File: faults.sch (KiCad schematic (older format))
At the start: 4 parts

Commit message: Adds todos.
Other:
- note added: "TODO(willjschmitt): Implement fault latching."
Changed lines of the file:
@@
 Wire Wire Line
 	5950 2000 6050 2000
+Text Notes 6700 1350 0    60   ~ 0
+TODO(willjschmitt): Implement fault latching.
 $EndSCHEMATC

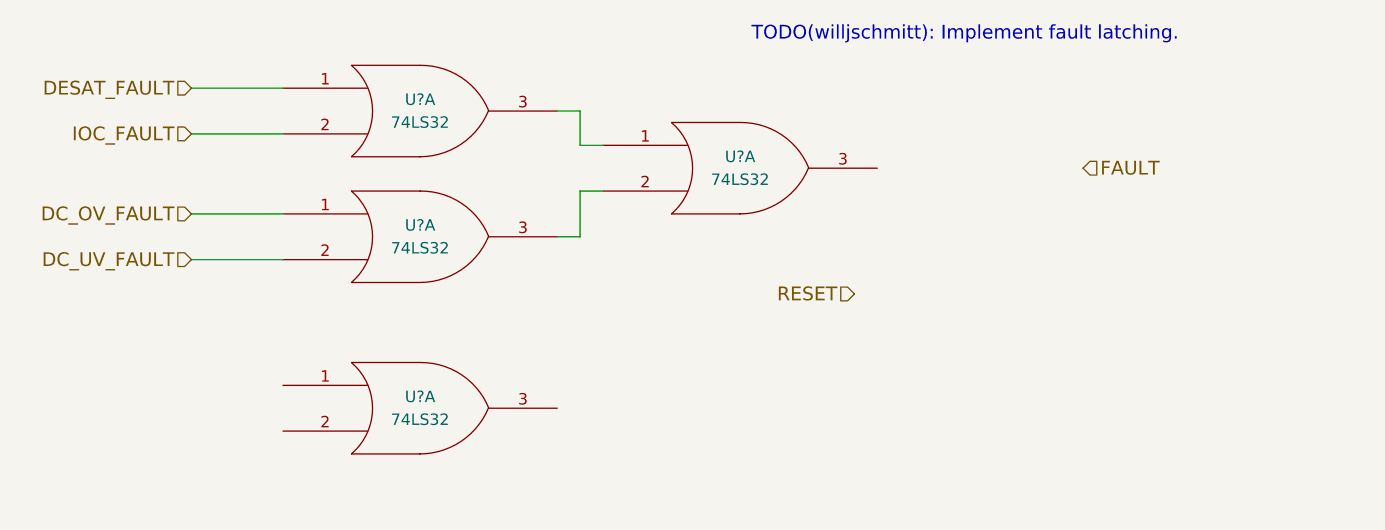
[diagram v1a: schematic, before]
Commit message: Adding latch to fault module.
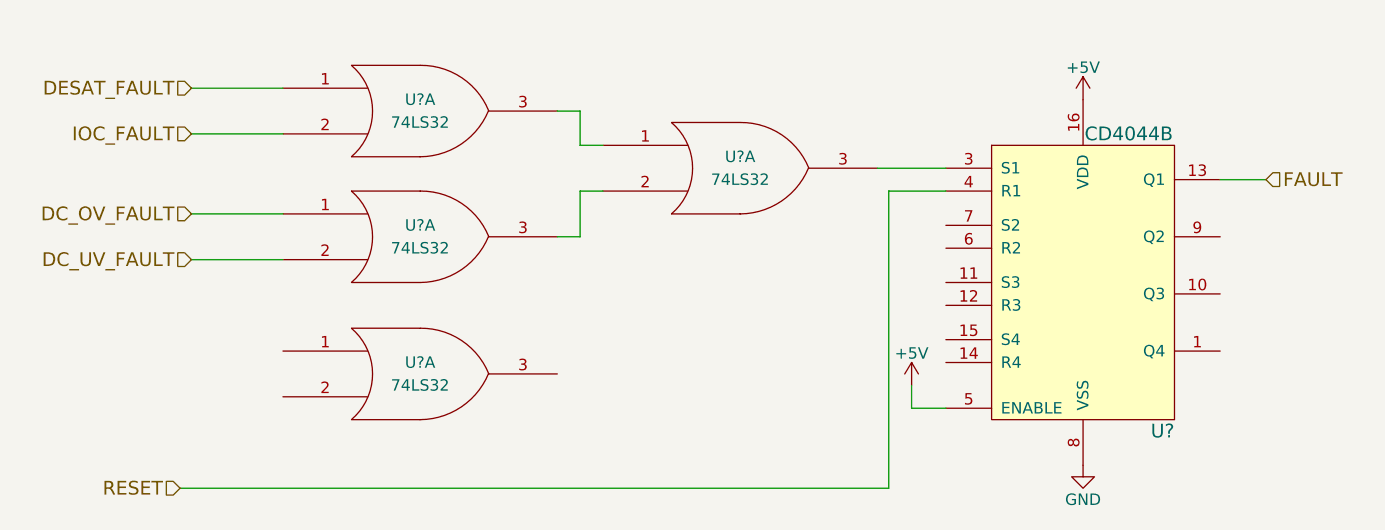
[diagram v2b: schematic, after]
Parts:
- added U?: CD4044B, symbol CD4044B
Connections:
- net FAULT: now also U?.13 (Q1)
- net GND: now also U?.8 (VSS)
- net RESET: now also U?.4 (R1)
- net at U?.3: now also U?.3 (S1)
- new net +5V: U?.16 (VDD), U?.5 (ENABLE)
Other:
- note removed: "TODO(willjschmitt): Implement fault latching."
- moved on the sheet: U?A
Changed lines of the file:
@@
 Text HLabel 4250 1550 0    60   Input ~ 0
 DESAT_FAULT
-Text HLabel 7150 2450 0    60   Input ~ 0
+Text HLabel 4200 3300 0    60   Input ~ 0
 RESET
-Text HLabel 8150 1900 2    60   Input ~ 0
+Text HLabel 8950 1950 2    60   Input ~ 0
 FAULT
 Text HLabel 4250 2100 0    60   Input ~ 0
@@
 L 74LS32 U?
 U 1 1 5AFAF32E
-P 5250 2950
-F 0 "U?" H 5250 3000 50  0000 C CNN
-F 1 "74LS32" H 5250 2900 50  0000 C CNN
-F 2 "" H 5250 2950 50  0001 C CNN
-F 3 "" H 5250 2950 50  0001 C CNN
-	1    5250 2950
+P 5250 2800
+F 0 "U?" H 5250 2850 50  0000 C CNN
+F 1 "74LS32" H 5250 2750 50  0000 C CNN
+F 2 "" H 5250 2800 50  0001 C CNN
+F 3 "" H 5250 2800 50  0001 C CNN
+	1    5250 2800
 	1    0    0    -1
 $EndComp
@@
 Wire Wire Line
 	5950 2000 6050 2000
-Text Notes 6700 1350 0    60   ~ 0
-TODO(willjschmitt): Implement fault latching.
+$Comp
+L CD4044B U?
+U 1 1 5AFE1E4B
+P 8150 2200
+F 0 "U?" H 8550 1350 60  0000 R CNN
+F 1 "CD4044B" H 8350 2650 60  0000 C CNN
+F 2 "" H 8150 2200 60  0001 C CNN
+F 3 "" H 8150 2200 60  0001 C CNN
+	1    8150 2200
+	1    0    0    -1
+$EndComp
+Wire Wire Line
+	4200 3300 7300 3300
+Wire Wire Line
+	7300 3300 7300 2000
+Wire Wire Line
+	7300 2000 7550 2000
+Wire Wire Line
+	7250 1900 7550 1900
+$Comp
+L +5V #PWR?
+U 1 1 5AFE2198
+P 8150 1600
+F 0 "#PWR?" H 8150 1450 50  0001 C CNN
+F 1 "+5V" H 8150 1740 50  0000 C CNN
+F 2 "" H 8150 1600 50  0001 C CNN
+F 3 "" H 8150 1600 50  0001 C CNN
+	1    8150 1600
+	1    0    0    -1
+$EndComp
+$Comp
+L GND #PWR?
+U 1 1 5AFE21F2
+P 8150 3200
+F 0 "#PWR?" H 8150 2950 50  0001 C CNN
+F 1 "GND" H 8150 3050 50  0000 C CNN
+F 2 "" H 8150 3200 50  0001 C CNN
+F 3 "" H 8150 3200 50  0001 C CNN
+	1    8150 3200
+	1    0    0    -1
+$EndComp
+Wire Wire Line
+	8950 1950 8750 1950
+$Comp
+L +5V #PWR?
+U 1 1 5AFE2A17
+P 7400 2850
+F 0 "#PWR?" H 7400 2700 50  0001 C CNN
+F 1 "+5V" H 7400 2990 50  0000 C CNN
+F 2 "" H 7400 2850 50  0001 C CNN
+F 3 "" H 7400 2850 50  0001 C CNN
+	1    7400 2850
+	1    0    0    -1
+$EndComp
+Wire Wire Line
+	7400 2850 7400 2950
+Wire Wire Line
+	7400 2950 7550 2950
 $EndSCHEMATC

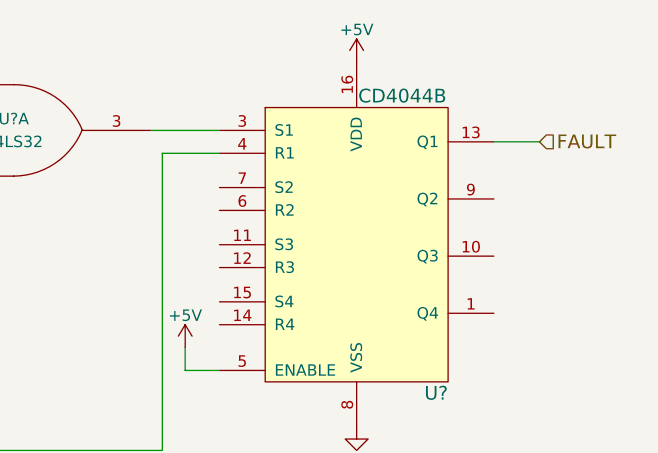
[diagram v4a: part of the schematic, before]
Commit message: Add fault lockout to relays.
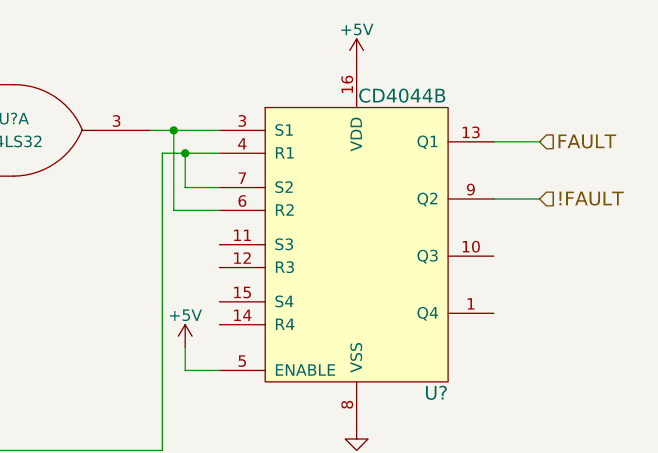
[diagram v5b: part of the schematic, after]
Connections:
- net RESET: now also U?.7 (S2)
- net at U?.3, U?.3 (S1): now also U?.6 (R2)
- net !FAULT: now reaches U?.9 (Q2)
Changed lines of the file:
@@
 Wire Wire Line
 	7400 2950 7550 2950
+Text HLabel 8950 2200 2    60   Input ~ 0
+!FAULT
+Wire Wire Line
+	8950 2200 8750 2200
+Wire Wire Line
+	7350 1900 7350 2250
+Wire Wire Line
+	7350 2250 7550 2250
+Connection ~ 7350 1900
+Wire Wire Line
+	7550 2150 7400 2150
+Wire Wire Line
+	7400 2150 7400 2000
+Connection ~ 7400 2000
 $EndSCHEMATC

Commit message: Annotate and add negative IOC faults.
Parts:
- gave numbers to parts that had none: 2
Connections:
- net DC_OV_FAULT: now also U7.4; no longer U7.1
- net DC_UV_FAULT: now also U7.5; no longer U7.2
- net at U7.3: now also U7.12; no longer U7.1
- net at U8.3 (S1), U8.6 (R2): now also U7.11; no longer U7.3
- new net: U7.13, U7.6
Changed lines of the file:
@@
 DC_UV_FAULT
 $Comp
-L 74LS32 U?
+L 74LS32 U7
 U 1 1 5AFAF319
 P 5250 1650
-F 0 "U?" H 5250 1700 50  0000 C CNN
+F 0 "U7" H 5250 1700 50  0000 C CNN
 F 1 "74LS32" H 5250 1600 50  0000 C CNN
 F 2 "" H 5250 1650 50  0001 C CNN
@@
 $EndComp
 $Comp
-L 74LS32 U?
-U 1 1 5AFAF320
+L 74LS32 U7
+U 2 1 5AFAF320
 P 5250 2200
-F 0 "U?" H 5250 2250 50  0000 C CNN
+F 0 "U7" H 5250 2250 50  0000 C CNN
 F 1 "74LS32" H 5250 2150 50  0000 C CNN
 F 2 "" H 5250 2200 50  0001 C CNN
 F 3 "" H 5250 2200 50  0001 C CNN
-	1    5250 2200
+	2    5250 2200
 	1    0    0    -1
 $EndComp
 $Comp
-L 74LS32 U?
-U 1 1 5AFAF327
+L 74LS32 U7
+U 4 1 5AFAF327
 P 6650 1900
-F 0 "U?" H 6650 1950 50  0000 C CNN
+F 0 "U7" H 6650 1950 50  0000 C CNN
 F 1 "74LS32" H 6650 1850 50  0000 C CNN
 F 2 "" H 6650 1900 50  0001 C CNN
 F 3 "" H 6650 1900 50  0001 C CNN
-	1    6650 1900
+	4    6650 1900
 	1    0    0    -1
 $EndComp
 $Comp
-L 74LS32 U?
-U 1 1 5AFAF32E
+L 74LS32 U7
+U 3 1 5AFAF32E
 P 5250 2800
-F 0 "U?" H 5250 2850 50  0000 C CNN
+F 0 "U7" H 5250 2850 50  0000 C CNN
 F 1 "74LS32" H 5250 2750 50  0000 C CNN
 F 2 "" H 5250 2800 50  0001 C CNN
 F 3 "" H 5250 2800 50  0001 C CNN
-	1    5250 2800
+	3    5250 2800
 	1    0    0    -1
 $EndComp
@@
 	5950 2000 6050 2000
 $Comp
-L CD4044B U?
+L CD4044B U8
 U 1 1 5AFE1E4B
 P 8150 2200
-F 0 "U?" H 8550 1350 60  0000 R CNN
+F 0 "U8" H 8550 1350 60  0000 R CNN
 F 1 "CD4044B" H 8350 2650 60  0000 C CNN
 F 2 "" H 8150 2200 60  0001 C CNN
@@
 	7250 1900 7550 1900
 $Comp
-L +5V #PWR?
+L +5V #PWR49
 U 1 1 5AFE2198
 P 8150 1600
-F 0 "#PWR?" H 8150 1450 50  0001 C CNN
+F 0 "#PWR49" H 8150 1450 50  0001 C CNN
 F 1 "+5V" H 8150 1740 50  0000 C CNN
 F 2 "" H 8150 1600 50  0001 C CNN
@@
 $EndComp
 $Comp
-L GND #PWR?
+L GND #PWR50
 U 1 1 5AFE21F2
 P 8150 3200
-F 0 "#PWR?" H 8150 2950 50  0001 C CNN
+F 0 "#PWR50" H 8150 2950 50  0001 C CNN
 F 1 "GND" H 8150 3050 50  0000 C CNN
 F 2 "" H 8150 3200 50  0001 C CNN
@@
 	8950 1950 8750 1950
 $Comp
-L +5V #PWR?
+L +5V #PWR48
 U 1 1 5AFE2A17
 P 7400 2850
-F 0 "#PWR?" H 7400 2700 50  0001 C CNN
+F 0 "#PWR48" H 7400 2700 50  0001 C CNN
 F 1 "+5V" H 7400 2990 50  0000 C CNN
 F 2 "" H 7400 2850 50  0001 C CNN
